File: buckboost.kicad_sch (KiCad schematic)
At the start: 22 parts, among them Q1 30V/20A_NFET, Q2 30V/20A_NFET, Q3 30V/20A_NFET, Q4 30V/20A_NFET, U1 LM5176PWP

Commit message: components: lock buckboost FETs, R5 SLOPE, and charger config-R values
Buckboost Q1-Q4:
- AON7544 (LCSC C315567), 30V/30A, 5mOhm@10V, DFN-8 3x3, 183k stock,
  ~$0.12 @ qty 1-49.  Extended tier — per feedback_assembly_tier_cost
  memory, that's fine (the cost cliff is Standard-assembly tier, not
  Extended library type).  At 5A steady x 5mOhm = 25mW per FET
  conduction loss, well under the 23W package limit.
- Symbol + footprint + 3D model imported via easyeda2kicad for C315567,
  same workflow as IP2326.

Buckboost R5 (SLOPE):
- Was 10k placeholder.  Set to 20k per LM5176 §9.3.7 slope-compensation
  calc.  Inductor downslope Sn = (Vin_max=12.6V / L=6.8uH) x
  Rcs=5mOhm = ~9.3 mV/us; required Se >= Sn/2 = 4.6 mV/us to avoid
  sub-harmonic oscillation.  20k is TI-EVM starting point at this
  Fsw/L combo; safe against sub-harmonic and leaves loop-tune headroom.
  Notes property records bench-verification guidance.

Charger config-R updates:
- R1 (VSET) 10k → 100k — IP2326 §10 default for 12.6V float on 3S.
- R8 (ISET) 10k → 33k — I_chg ≈ 66/R_iset (kOhm) → 33k = 2A charge,
  0.67C for a 3Ah 3S pack.  Was 10k which would have set an
  unsafe ~6.6A charge rate.
- R2, R3, R4, R5, R6, R9, R10, R7 already at IP2326-typical values
  (verified via table in commit thread); no change needed.

Full-project ERC: 0 errors, 33 cosmetic warnings.  The 2 leftover
"SOIC-8 footprint not found" warnings from the placeholder Device:
Q_NMOS symbols are gone.

Co-Authored-By: Claude Opus 4.7 <noreply@anthropic.com>
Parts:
- Q1, Q2, Q3, Q4: value 30V/20A_NFET -> AON7544; footprint (none) -> power_module_lib:DFN-8_L3.3-W3.3-P0.65-BL-2; LCSC (none) -> C315567; MPN (none) -> AON7544; Manufacturer (none) -> Alpha & Omega Semi
- R5: value 10k -> 20k; Notes (none) -> Slope-comp per LM5176 §9.3.7 with Fsw=500kHz, L=6.8uH, Rcs=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

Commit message: sourcing: lock LCSC + MPN + Manufacturer + Footprint for every remaining BOM line
Applied JLCPCB picks (LCSC number + manufacturer part number + tuned
footprint) across all four sub-sheets — 72 components total.  Every
placed component now carries LCSC, MPN, and Manufacturer properties;
the built-in Value/Footprint fields point to the exact JLCPCB stock
unit for that pick.

Highlights:
- ICs (Preferred where available, Extended otherwise):
    U1(bms)      BQ7692003PWR   C601650    TSSOP-20
    U1(charger)  IP2326         C2832094   VQFN-24 EP4x4
    U1(input)    CH224K         C970725    ESSOP-10
    U1(bckbst)   LM5176PWPR     C442493    HTSSOP-28
- Diodes + TVS (all Preferred tier):
    D1(input)    SRV05-4        C7420376   SOT-23-6   (622K stock)
    D2(input)    SMAJ12A        C19077531  SMA        ( 33K stock)
    D1-3(bms)    SMAJ15A        C19077535  SMA        (174K stock)
- Power passives:
    L1(bckbst)   6.8uH 5A       C167221    FXL0630-6R8-M  7x6.6mm
    L1(charger)  2.2uH 4.8A     C602029    FHD4020S-2R2MT 4x4mm
    FB1(input)   600R@100MHz    C139183    CBW160808U601T 0603 (1A)
    R9(bms)      5mR 2W ±1%     C185817    RLM25FEER005   2512
- Bulk passives — Uniohm 0603WAF series, ±1%, high stock.  All caps
  Samsung/Yageo 0603 or 0805 ceramic.  Reused Q1-Q4 = AON7544
  (already locked at 9120877) for bms.Q1/Q2 too — same part
  covers 30V/20A pack-return FET stack.

Effect on pre-fab readiness (kicad-happy):
- SS-001 error CLEARED — 1/34 MPN coverage was blocking pre-fab;
  now 34/34 (100%).
- DS-002 warning shifted: was "no datasheets" (2/34 MPNs), now
  "no datasheets dir" (34/34 MPNs).  Non-blocking; datasheet PDFs
  are nice-to-have but the review can proceed without them.
- 1 remaining error PP-001 (LM5176_VCC no DC source) is a false
  positive: KiCad library symbol declares VCC as power_in but it's
  actually the LM5176's internal 5V LDO OUTPUT.  Accepted as-is.

Full-project ERC still 0 errors.  Schematic is now sourcing-clean
and ready for 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
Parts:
- C1, C10, C11, C2: LCSC (none) -> C45783; MPN (none) -> CL21A226MAQNNNE; Manufacturer (none) -> SAMSUNG
- C3: LCSC (none) -> C23630; MPN (none) -> CL10A225KO8NNNC; Manufacturer (none) -> SAMSUNG
- C4: LCSC (none) -> C15849; MPN (none) -> CL10A105KB8NNNC; Manufacturer (none) -> SAMSUNG
- C5, C6: LCSC (none) -> C14663; MPN (none) -> CC0603KRX7R9BB104; Manufacturer (none) -> YAGEO
- C7: LCSC (none) -> C5137477; MPN (none) -> FCC0603B103K500CT; Manufacturer (none) -> FH
- C8: LCSC (none) -> C53987; MPN (none) -> 0603B472K500NT; Manufacturer (none) -> FH
- L1: footprint (none) -> Inductor_SMD:L_Sumida_CDMC6D28; LCSC (none) -> C167221; MPN (none) -> FXL0630-6R8-M; Manufacturer (none) -> FH (Guangdong Fenghua)
- R1: LCSC (none) -> C25805; MPN (none) -> 0603WAF1103T5E; Manufacturer (none) -> Uniohm
- R2: LCSC (none) -> C25804; MPN (none) -> 0603WAF1002T5E; Manufacturer (none) -> Uniohm
- R3, R5: LCSC (none) -> C4184; MPN (none) -> 0603WAF2002T5E; Manufacturer (none) -> Uniohm
- R4: LCSC (none) -> C12447; MPN (none) -> 0603WAF4022T5E; Manufacturer (none) -> Uniohm
- R6: LCSC (none) -> C25803; MPN (none) -> 0603WAF1003T5E; Manufacturer (none) -> Uniohm
- U1: footprint (none) -> Package_SO:HTSSOP-28-1EP_4.4x9.7mm_P0.65mm_EP3.4x9.5mm_ThermalVias; LCSC (none) -> C442493; MPN (none) -> LM5176PWPR; Manufacturer (none) -> Texas Instruments

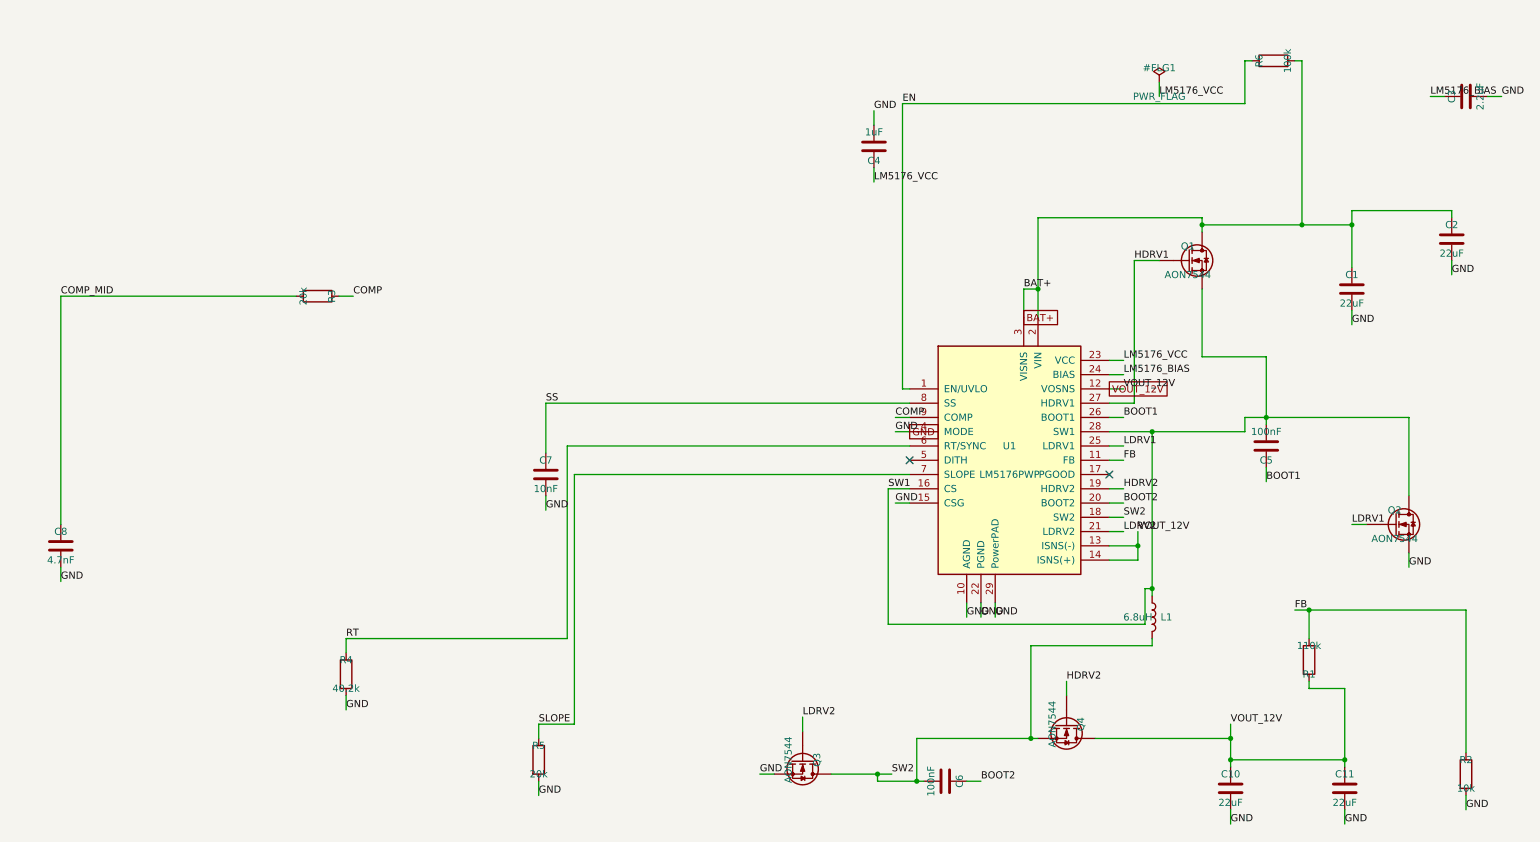
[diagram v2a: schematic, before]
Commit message: sheets: hierarchical ref disambiguation via annotate_schematic
Every sub-sheet symbol now carries a `_{SHEETNAME}{instance_num}` suffix so
refs are globally unique across the hierarchy.  76 refs rewritten:
  bms:       27 (e.g. U1 → U1_BMS1,      Q1 → Q1_BMS1)
  charger:   19 (e.g. U1 → U1_CHARGER1,  R7 → R7_CHARGER1)
  input:      8 (e.g. U1 → U1_INPUT1,    J1 → J1_INPUT1)
  buckboost: 22 (e.g. U1 → U1_BUCKBOOST1,Q1 → Q1_BUCKBOOST1)

Fixes kicad-cli's `schematic has annotation errors` warning which previously
caused BOM export to collapse the four different U1's (BQ76920 + IP2326 +
CH224K + LM5176) into a single row with comma-joined values.

bom_step1.csv committed alongside as the post-disambiguation baseline —
38 grouped rows, 100% LCSC/MPN coverage.

Applied via the new `annotate_schematic` hierarchical pass shipped in
KiCAD-MCP-Server c529efa on develop.  See NOTES.md for the mid-session
handoff block and memory `feedback_hierarchical_annotate`.

Co-Authored-By: Claude Opus 4.7 <noreply@anthropic.com>
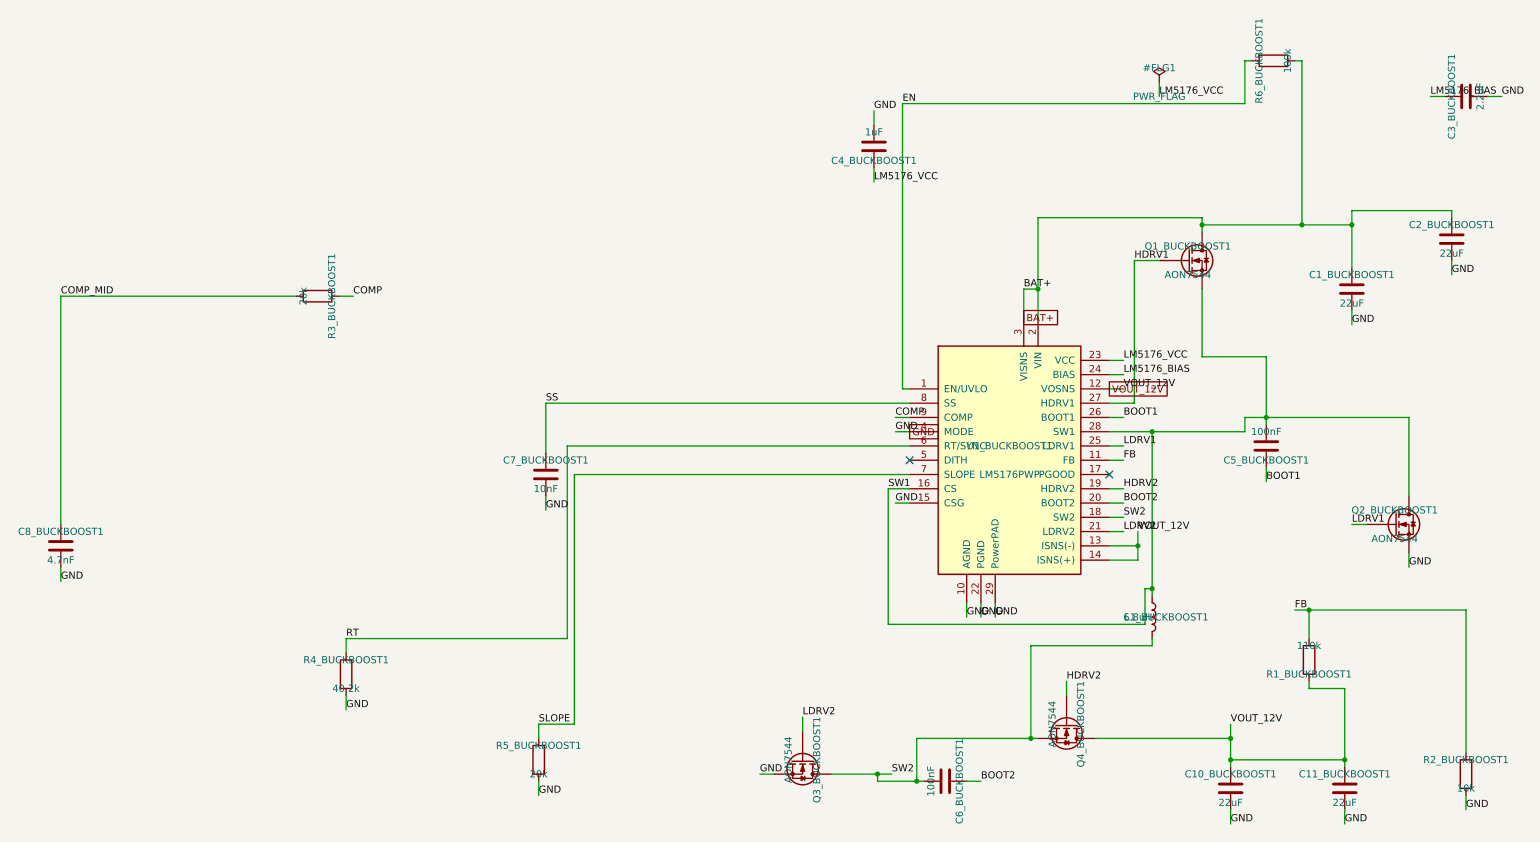
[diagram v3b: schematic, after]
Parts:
- renumbered C10 to C10_BUCKBOOST1, C11 to C11_BUCKBOOST1, C1 to C1_BUCKBOOST1, C2 to C2_BUCKBOOST1, C3 to C3_BUCKBOOST1, C4 to C4_BUCKBOOST1, C5 to C5_BUCKBOOST1, C6 to C6_BUCKBOOST1, C7 to C7_BUCKBOOST1, C8 to C8_BUCKBOOST1, L1 to L1_BUCKBOOST1, Q1 to Q1_BUCKBOOST1, Q2 to Q2_BUCKBOOST1, Q3 to Q3_BUCKBOOST1, Q4 to Q4_BUCKBOOST1, R1 to R1_BUCKBOOST1, R2 to R2_BUCKBOOST1, R3 to R3_BUCKBOOST1, R4 to R4_BUCKBOOST1, R5 to R5_BUCKBOOST1, R6 to R6_BUCKBOOST1, U1 to U1_BUCKBOOST1

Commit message: Step 2: complete Footprint set + sync 76 footprints to .kicad_pcb
Fill in the Footprint properties that were missing from the prior
sourcing pass, and sync everything to the PCB.

Footprint updates on the schematic:
- 35 passives got their Footprint assigned by value (0603 for R/C ≤1uF,
  0805 for 10uF/22uF caps).
- BAT1_BMS1 → power_module_lib:BAT-SMD_BH-18650-B5BA016 (was truncated).
- L1_BUCKBOOST1 → Inductor_SMD:L_Sumida_CDMC6D28_7.25x6.5mm (needed the
  size suffix so KiCad can resolve the .kicad_mod file).

Sync result: 76/76 footprints imported, 60 nets added, 245 pads assigned,
0 import errors.  Unmatched pads reported are all intentional NCs per
REQUIREMENTS.md (USB-C D+/D-, CH224K SBU/CFG, SRV05-4 unused ESD channels).

The footprints are at the default y=-140..-20 auto-import grid; no
placement work yet.  Next step is add_board_outline + set_design_rules.

For discoverability going forward, the pre-sync gap gets caught by
check_sourcing_readiness (KiCAD-MCP-Server fa93ba9 on develop) rather
than having to reset the .kicad_pcb after every retro-fill of an empty
Footprint property.

Co-Authored-By: Claude Opus 4.7 <noreply@anthropic.com>
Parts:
- C10_BUCKBOOST1, C11_BUCKBOOST1, C1_BUCKBOOST1, C2_BUCKBOOST1: footprint (none) -> Capacitor_SMD:C_0805_2012Metric
- C3_BUCKBOOST1, C4_BUCKBOOST1, C5_BUCKBOOST1, C6_BUCKBOOST1, C7_BUCKBOOST1, C8_BUCKBOOST1: footprint (none) -> Capacitor_SMD:C_0603_1608Metric
- L1_BUCKBOOST1: footprint Inductor_SMD:L_Sumida_CDMC6D28 -> Inductor_SMD:L_Sumida_CDMC6D28_7.25x6.5mm
- R1_BUCKBOOST1, R2_BUCKBOOST1, R3_BUCKBOOST1, R4_BUCKBOOST1, R5_BUCKBOOST1, R6_BUCKBOOST1: footprint (none) -> Resistor_SMD:R_0603_1608Metric

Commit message: Step 3+4 WIP: board outline, 4-layer stackup, decoupling spring classes, initial placement pass
Step 3 (board mechanics)
- Edge.Cuts rectangle 100x70 mm (BAT1 alone is 82.3x56.8 so 60x80 in
  the pre-session NOTES was too small)
- 4-layer stackup: added In1.Cu (GND plane) + In2.Cu (PWR plane)
- Design rules tightened: clearance 0.15, minTrackWidth 0.15,
  minViaDiameter 0.45, viaDrill 0.3

Step 4 (WIP — placement)
- 13 Pin_Spring_Class:{pad} = {"IC.pin": "DECOUPLING"} assignments on
  bypass caps across bms/charger/buckboost.  Every IC's power/reservoir/
  bootstrap cap now has an explicit DECOUPLING target so the auto-placer
  parks it right next to the IC pin instead of drifting off with the
  power-rail centroid:
    C7_BMS1        -> BQ76920 CAP1 (pin 7, charge pump reservoir)
    C5_BMS1        -> BQ76920 REGOUT bypass (pin 8)
    C6_BMS1        -> BQ76920 BAT+ sense
    C1..C4_BMS1    -> BQ76920 VCn sense RC filters
    C3_BUCKBOOST1  -> LM5176 BIAS bypass (pin 24, 2.2uF)
    C4_BUCKBOOST1  -> LM5176 VCC LDO bypass (pin 23, 1uF)
    C5_BUCKBOOST1  -> LM5176 BOOT1 bootstrap (pin 26)
    C6_BUCKBOOST1  -> LM5176 BOOT2 bootstrap (pin 20)
    C7_BUCKBOOST1  -> LM5176 SS (pin 8)
    C5_CHARGER1    -> IP2326 BST_CAP (pin 14)
- Initial relax_placement pass with 7 locked anchors (2 headers + BAT1 +
  4 ICs).  Not a shippable layout yet: USB-C is backwards, I2C header
  overlaps BAT1's B.Cu pad zone, Q1..Q4 + L1 (buck-boost power stage)
  scattered from LM5176.  Left as a starting point for hand-refinement.
- TH1_BMS1 (pack thermistor) flipped to B.Cu for proximity to the
  cells — final position to be set by hand.

Co-Authored-By: Claude Opus 4.7 <noreply@anthropic.com>
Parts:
- C3_BUCKBOOST1: Pin_Spring_Class:1 (none) -> {"U1_BUCKBOOST1.24":"DECOUPLING"}
- C4_BUCKBOOST1: Pin_Spring_Class:1 (none) -> {"U1_BUCKBOOST1.23":"DECOUPLING"}
- C5_BUCKBOOST1: Pin_Spring_Class:1 (none) -> {"U1_BUCKBOOST1.26":"DECOUPLING"}
- C6_BUCKBOOST1: Pin_Spring_Class:1 (none) -> {"U1_BUCKBOOST1.20":"DECOUPLING"}
- C7_BUCKBOOST1: Pin_Spring_Class:1 (none) -> {"U1_BUCKBOOST1.8":"DECOUPLING"}

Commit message: Fix EN cross-sheet collision + tag charger VSYS/BAT decoupling caps
EN was accidentally shared across charger and buckboost

Both sheets carried a local label named "EN" — kicad-cli sch export
netlist correctly namespaces these as /charger/EN and /buckboost/EN, but
the .kicad_pcb had ONE net "EN" (net 42) with all four pads collapsed
into it: IP2326 pin 11 was electrically tied to LM5176 pin 1 through PCB
copper.  IP2326.EN is pulled up to VBUS_9V via R9_CHARGER1 (9V rail),
LM5176.EN is pulled up to BAT+ via R6_BUCKBOOST1 (12V rail); shorting
them would fight the pull-ups and give indeterminate enable behaviour.

Renamed the labels to make them unambiguously distinct:

  charger:   EN → CHG_EN
  buckboost: EN → BB_EN

Post-sync verification:
  EN     — 0 pads
  CHG_EN — R9_CHARGER1.2, U1_CHARGER1.11
  BB_EN  — R6_BUCKBOOST1.1, U1_BUCKBOOST1.1

Underlying sync_schematic_to_board bug (collapsing same-named local
labels across sheets when the kicad-cli netlist keeps them separate) is
filed for follow-up on the MCP-server side.  Sweep for other cross-sheet
collisions: only VBUS_9V (input↔charger, intentional) was found.

C2/C3/C4_CHARGER1 decoupling tags added

The earlier decoupling analyser only spotted caps whose non-power pad
lands on a *single* IC pin AND whose ground pad is literal "GND".  It
missed:

  C2_CHARGER1 (22uF) — VSYS bulk cap → tag DECOUPLING to U1_CHARGER1.19
  C3_CHARGER1 (22uF) — VSYS bulk cap → tag DECOUPLING to U1_CHARGER1.20
  C4_CHARGER1 (10uF) — BAT+ input cap → tag DECOUPLING to U1_CHARGER1.21

Distributes across VSYS pins 19+20 so the two 22uF caps don't fight for
the same target pin.  C4 was floating in the last relax pass because its
BAT+ pad was PLANE-classified (via META1 singleton) and GND is a
44-node auto-PLANE; explicit DECOUPLING gives it a target to anchor to.

Co-Authored-By: Claude Opus 4.7 <noreply@anthropic.com>
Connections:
- net EN renamed BB_EN

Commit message: buckboost: tag C1/C2/C10/C11 bulk caps as DECOUPLING to LM5176 VIN/VOUT pins
The 22uF input (C1/C2) and output (C10/C11) bulk caps had both pins on
PLANE-classified nets (BAT+ + GND for input, VOUT_12V + GND for output —
all three are PLANE via the META1 mcp_spring_classes.nets singleton), so
the placer had zero attraction pulling them toward LM5176 and they
drifted to the periphery of the buckboost cluster.

Tagged as DECOUPLING to specific IC pins, distributed so the two input
caps don't fight for the same target and same for the outputs:

  C1_BUCKBOOST1.1  → LM5176.2  (VIN #1)
  C2_BUCKBOOST1.1  → LM5176.3  (VIN #2)
  C10_BUCKBOOST1.1 → LM5176.12 (VOUT #1)
  C11_BUCKBOOST1.1 → LM5176.13 (VOUT #2)

LM5176 datasheet §10.1 requires these right up against the pins for
low switching-loop inductance.  A future re-placement / relax pass
will park them there.

Same class of miss as the earlier C2/C3/C4_CHARGER1 fix — bulk caps on
multi-node power rails are the exact case the retroactive analyser
missed and only the placement-time authoring convention catches
reliably (see feedback_tag_spring_class_at_placement).

Co-Authored-By: Claude Opus 4.7 <noreply@anthropic.com>
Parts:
- C10_BUCKBOOST1: Pin_Spring_Class:1 (none) -> {"U1_BUCKBOOST1.12":"DECOUPLING"}
- C11_BUCKBOOST1: Pin_Spring_Class:1 (none) -> {"U1_BUCKBOOST1.13":"DECOUPLING"}
- C1_BUCKBOOST1: Pin_Spring_Class:1 (none) -> {"U1_BUCKBOOST1.2":"DECOUPLING"}
- C2_BUCKBOOST1: Pin_Spring_Class:1 (none) -> {"U1_BUCKBOOST1.3":"DECOUPLING"}
